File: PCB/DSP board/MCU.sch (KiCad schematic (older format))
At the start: 12 parts, among them J1 01x06 male SMD, U1 STM32H743II, Y1 ABS05-32.768, Y2 CX2016DB16000

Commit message: Schematics + Footprints Rev.1
Ready to route.
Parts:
- C1, C2, C3, C4, C5: footprint (none) -> Capacitors_SMD:C_0603
- J1: footprint (none) -> Pin_Headers:Pin_Header_Straight_1x06_Pitch2.54mm_SMD_Pin1Right
- R1: value 47k -> 12k; footprint (none) -> Resistors_SMD:R_0603
- R2: footprint (none) -> Resistors_SMD:R_0603
- S1: value Switch_SPST_4Pin -> FSM4JSMATR; footprint (none) -> Switch:FSM4JSMATR
- U1: footprint (none) -> Housings_QFP:LQFP-176_24x24mm_Pitch0.5mm
- Y1: footprint (none) -> Crystals:Crystal_SMD_MicroCrystal_CM9V-T1A-2pin_1.6x1.0mm
- Y2: footprint (none) -> Crystals:Crystal_SMD_2016-4pin_2.0x1.6mm
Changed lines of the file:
@@
 F 0 "U1" H 1600 3475 60  0000 C CNN
 F 1 "STM32H743II" H 1900 925 60  0000 C CNN
-F 2 "" H 1900 925 60  0001 C CNN
+F 2 "Housings_QFP:LQFP-176_24x24mm_Pitch0.5mm" H 1900 925 60  0001 C CNN
 F 3 "" H 1900 925 60  0001 C CNN
 	1    1900 2225
@@
 F 0 "U1" H 1600 6275 60  0000 C CNN
 F 1 "STM32H743II" H 1900 3725 60  0000 C CNN
-F 2 "" H 1900 3725 60  0001 C CNN
+F 2 "Housings_QFP:LQFP-176_24x24mm_Pitch0.5mm" H 1900 3725 60  0001 C CNN
 F 3 "" H 1900 3725 60  0001 C CNN
 	2    1900 5025
@@
 F 0 "U1" H 3650 3475 60  0000 C CNN
 F 1 "STM32H743II" H 3950 925 60  0000 C CNN
-F 2 "" H 3950 925 60  0001 C CNN
+F 2 "Housings_QFP:LQFP-176_24x24mm_Pitch0.5mm" H 3950 925 60  0001 C CNN
 F 3 "" H 3950 925 60  0001 C CNN
 	3    3950 2225
@@
 F 0 "U1" H 3700 6275 60  0000 C CNN
 F 1 "STM32H743II" H 4000 3725 60  0000 C CNN
-F 2 "" H 4000 3725 60  0001 C CNN
+F 2 "Housings_QFP:LQFP-176_24x24mm_Pitch0.5mm" H 4000 3725 60  0001 C CNN
 F 3 "" H 4000 3725 60  0001 C CNN
 	4    4000 5025
@@
 F 0 "U1" H 5700 3475 60  0000 C CNN
 F 1 "STM32H743II" H 6000 925 60  0000 C CNN
-F 2 "" H 6000 925 60  0001 C CNN
+F 2 "Housings_QFP:LQFP-176_24x24mm_Pitch0.5mm" H 6000 925 60  0001 C CNN
 F 3 "" H 6000 925 60  0001 C CNN
 	5    6000 2225
@@
 F 0 "U1" H 5750 6375 60  0000 C CNN
 F 1 "STM32H743II" H 6050 3825 60  0000 C CNN
-F 2 "" H 6050 3825 60  0001 C CNN
+F 2 "Housings_QFP:LQFP-176_24x24mm_Pitch0.5mm" H 6050 3825 60  0001 C CNN
 F 3 "" H 6050 3825 60  0001 C CNN
 	6    6050 5125
@@
 F 0 "U1" H 7700 3475 60  0000 C CNN
 F 1 "STM32H743II" H 8000 925 60  0000 C CNN
-F 2 "" H 8000 925 60  0001 C CNN
+F 2 "Housings_QFP:LQFP-176_24x24mm_Pitch0.5mm" H 8000 925 60  0001 C CNN
 F 3 "" H 8000 925 60  0001 C CNN
 	7    8000 2225
@@
 F 0 "U1" H 7750 6375 60  0000 C CNN
 F 1 "STM32H743II" H 8050 3825 60  0000 C CNN
-F 2 "" H 8050 3825 60  0001 C CNN
+F 2 "Housings_QFP:LQFP-176_24x24mm_Pitch0.5mm" H 8050 3825 60  0001 C CNN
 F 3 "" H 8050 3825 60  0001 C CNN
 	8    8050 5125
@@
 F 0 "U1" H 10400 3450 60  0000 C CNN
 F 1 "STM32H743II" H 10700 900 60  0000 C CNN
-F 2 "" H 10700 900 60  0001 C CNN
+F 2 "Housings_QFP:LQFP-176_24x24mm_Pitch0.5mm" H 10700 900 60  0001 C CNN
 F 3 "" H 10700 900 60  0001 C CNN
 	9    10700 2200
@@
 F 0 "C1" V 2725 3250 50  0000 L CNN
 F 1 "18pF" V 2625 2950 50  0000 L CNN
-F 2 "" H 2675 3200 50  0001 C CNN
+F 2 "Capacitors_SMD:C_0603" H 2675 3200 50  0001 C CNN
 F 3 "" H 2675 3200 50  0001 C CNN
 	1    2675 3200
@@
 F 0 "C2" V 2725 3450 50  0000 L CNN
 F 1 "18pF" V 2625 3150 50  0000 L CNN
-F 2 "" H 2675 3400 50  0001 C CNN
+F 2 "Capacitors_SMD:C_0603" H 2675 3400 50  0001 C CNN
 F 3 "" H 2675 3400 50  0001 C CNN
 	1    2675 3400
@@
 $EndComp
 $Comp
-L GND #PWR7
+L GND #PWR07
 U 1 1 5AABABFC
 P 2475 3500
-F 0 "#PWR7" H 2475 3250 50  0001 C CNN
+F 0 "#PWR07" H 2475 3250 50  0001 C CNN
 F 1 "GND" H 2475 3350 50  0000 C CNN
 F 2 "" H 2475 3500 50  0001 C CNN
@@
 F 0 "Y2" V 7000 3875 50  0000 L CNN
 F 1 "CX2016DB16000" V 6800 3825 50  0000 L CNN
-F 2 "" H 7150 4075 50  0001 C CNN
+F 2 "Crystals:Crystal_SMD_2016-4pin_2.0x1.6mm" H 7150 4075 50  0001 C CNN
 F 3 "" H 7150 4075 50  0001 C CNN
 	1    7150 4075
@@
 $EndComp
 $Comp
-L GND #PWR9
+L GND #PWR08
 U 1 1 5AABD6EF
 P 7350 4075
-F 0 "#PWR9" H 7350 3825 50  0001 C CNN
+F 0 "#PWR08" H 7350 3825 50  0001 C CNN
 F 1 "GND" H 7350 3925 50  0000 C CNN
 F 2 "" H 7350 4075 50  0001 C CNN
@@
 F 0 "Y1" V 3000 3400 50  0000 C CNN
 F 1 "ABS05-32.768" V 3300 3350 50  0000 C CNN
-F 2 "" H 3050 3300 50  0001 C CNN
+F 2 "Crystals:Crystal_SMD_MicroCrystal_CM9V-T1A-2pin_1.6x1.0mm" H 3050 3300 50  0001 C CNN
 F 3 "" H 3050 3300 50  0001 C CNN
 	1    3050 3300
@@
 F 0 "C3" V 6850 4025 50  0000 L CNN
 F 1 "18pF" V 6750 3725 50  0000 L CNN
-F 2 "" H 6800 3975 50  0001 C CNN
+F 2 "Capacitors_SMD:C_0603" H 6800 3975 50  0001 C CNN
 F 3 "" H 6800 3975 50  0001 C CNN
 	1    6800 3975
@@
 F 0 "C4" V 6850 4225 50  0000 L CNN
 F 1 "18pF" V 6750 3925 50  0000 L CNN
-F 2 "" H 6800 4175 50  0001 C CNN
+F 2 "Capacitors_SMD:C_0603" H 6800 4175 50  0001 C CNN
 F 3 "" H 6800 4175 50  0001 C CNN
 	1    6800 4175
@@
 $EndComp
 $Comp
-L GND #PWR8
+L GND #PWR09
 U 1 1 5AABF2BF
 P 6600 4275
-F 0 "#PWR8" H 6600 4025 50  0001 C CNN
+F 0 "#PWR09" H 6600 4025 50  0001 C CNN
 F 1 "GND" H 6600 4125 50  0000 C CNN
 F 2 "" H 6600 4275 50  0001 C CNN
@@
 F 0 "C5" H 8875 3275 50  0000 L CNN
 F 1 "100nF" H 8850 3125 50  0000 L CNN
-F 2 "" H 9100 3200 50  0001 C CNN
+F 2 "Capacitors_SMD:C_0603" H 9100 3200 50  0001 C CNN
 F 3 "" H 9100 3200 50  0001 C CNN
 	1    9100 3200
@@
 P 9300 3200
 F 0 "R1" H 9200 3275 50  0000 C CNN
-F 1 "47k" V 9300 3200 50  0000 C CNN
-F 2 "" V 9230 3200 50  0001 C CNN
+F 1 "12k" V 9300 3200 50  0000 C CNN
+F 2 "Resistors_SMD:R_0603" V 9230 3200 50  0001 C CNN
 F 3 "" H 9300 3200 50  0001 C CNN
 	1    9300 3200
@@
 Connection ~ 9100 2900
 $Comp
-L GND #PWR10
+L GND #PWR010
 U 1 1 5AAD2FCE
 P 9200 3475
-F 0 "#PWR10" H 9200 3225 50  0001 C CNN
+F 0 "#PWR010" H 9200 3225 50  0001 C CNN
 F 1 "GND" H 9200 3325 50  0000 C CNN
 F 2 "" H 9200 3475 50  0001 C CNN
@@
 F 0 "J1" H 10525 4375 50  0000 C CNN
 F 1 "01x06 male SMD" H 10475 3700 50  0000 C CNN
-F 2 "" H 10525 4075 50  0001 C CNN
+F 2 "Pin_Headers:Pin_Header_Straight_1x06_Pitch2.54mm_SMD_Pin1Right" H 10525 4075 50  0001 C CNN
 F 3 "" H 10525 4075 50  0001 C CNN
 	1    10525 4075
@@
 	10325 3875 10100 3875
 $Comp
-L GND #PWR11
+L GND #PWR011
 U 1 1 5AB64D9A
 P 10250 4075
-F 0 "#PWR11" H 10250 3825 50  0001 C CNN
+F 0 "#PWR011" H 10250 3825 50  0001 C CNN
 F 1 "GND" V 10250 3800 50  0000 C CNN
 F 2 "" H 10250 4075 50  0001 C CNN
@@
 P 10200 4950
 F 0 "S1" V 10475 4950 60  0000 C CNN
-F 1 "Switch_SPST_4Pin" V 9950 4925 60  0000 C CNN
-F 2 "" H 10000 5050 60  0001 C CNN
+F 1 "FSM4JSMATR" V 9950 4925 60  0000 C CNN
+F 2 "Switch:FSM4JSMATR" H 10000 5050 60  0001 C CNN
 F 3 "" H 10000 5050 60  0001 C CNN
 	1    10200 4950
@@
 F 0 "R2" V 10780 5100 50  0000 C CNN
 F 1 "820R" V 10700 5100 50  0000 C CNN
-F 2 "" V 10630 5100 50  0001 C CNN
+F 2 "Resistors_SMD:R_0603" V 10630 5100 50  0001 C CNN
 F 3 "" H 10700 5100 50  0001 C CNN
 	1    10700 5100
@@
 $EndComp
 $Comp
-L GND #PWR12
+L GND #PWR012
 U 1 1 5AB64DB1
 P 10925 5150
-F 0 "#PWR12" H 10925 4900 50  0001 C CNN
+F 0 "#PWR012" H 10925 4900 50  0001 C CNN
 F 1 "GND" H 10925 5000 50  0000 C CNN
 F 2 "" H 10925 5150 50  0001 C CNN

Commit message: Schematics & PCB
Schematics update - ERC error fixing
PCB - setup & PCB outline
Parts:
- renumbered C1 to C201, C2 to C202, C3 to C203, C4 to C204, C5 to C205, J1 to J201, R1 to R201, R2 to R202, S1 to S201, U1 to U201, Y1 to Y201, Y2 to Y202
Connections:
- no-connect marks 0 -> 14
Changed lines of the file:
@@
 $EndSheet
 $Comp
-L STM32H743II U1
+L STM32H743II U201
 U 1 1 5AAA3D93
 P 1900 2225
-F 0 "U1" H 1600 3475 60  0000 C CNN
+F 0 "U201" H 1600 3475 60  0000 C CNN
 F 1 "STM32H743II" H 1900 925 60  0000 C CNN
 F 2 "Housings_QFP:LQFP-176_24x24mm_Pitch0.5mm" H 1900 925 60  0001 C CNN
@@
 $EndComp
 $Comp
-L STM32H743II U1
+L STM32H743II U201
 U 2 1 5AAA3F85
 P 1900 5025
-F 0 "U1" H 1600 6275 60  0000 C CNN
+F 0 "U201" H 1600 6275 60  0000 C CNN
 F 1 "STM32H743II" H 1900 3725 60  0000 C CNN
 F 2 "Housings_QFP:LQFP-176_24x24mm_Pitch0.5mm" H 1900 3725 60  0001 C CNN
@@
 $EndComp
 $Comp
-L STM32H743II U1
+L STM32H743II U201
 U 3 1 5AAA4068
 P 3950 2225
-F 0 "U1" H 3650 3475 60  0000 C CNN
+F 0 "U201" H 3650 3475 60  0000 C CNN
 F 1 "STM32H743II" H 3950 925 60  0000 C CNN
 F 2 "Housings_QFP:LQFP-176_24x24mm_Pitch0.5mm" H 3950 925 60  0001 C CNN
@@
 $EndComp
 $Comp
-L STM32H743II U1
+L STM32H743II U201
 U 4 1 5AAA418D
 P 4000 5025
-F 0 "U1" H 3700 6275 60  0000 C CNN
+F 0 "U201" H 3700 6275 60  0000 C CNN
 F 1 "STM32H743II" H 4000 3725 60  0000 C CNN
 F 2 "Housings_QFP:LQFP-176_24x24mm_Pitch0.5mm" H 4000 3725 60  0001 C CNN
@@
 $EndComp
 $Comp
-L STM32H743II U1
+L STM32H743II U201
 U 5 1 5AAA4260
 P 6000 2225
-F 0 "U1" H 5700 3475 60  0000 C CNN
+F 0 "U201" H 5700 3475 60  0000 C CNN
 F 1 "STM32H743II" H 6000 925 60  0000 C CNN
 F 2 "Housings_QFP:LQFP-176_24x24mm_Pitch0.5mm" H 6000 925 60  0001 C CNN
@@
 $EndComp
 $Comp
-L STM32H743II U1
+L STM32H743II U201
 U 6 1 5AAA44FA
 P 6050 5125
-F 0 "U1" H 5750 6375 60  0000 C CNN
+F 0 "U201" H 5750 6375 60  0000 C CNN
 F 1 "STM32H743II" H 6050 3825 60  0000 C CNN
 F 2 "Housings_QFP:LQFP-176_24x24mm_Pitch0.5mm" H 6050 3825 60  0001 C CNN
@@
 $EndComp
 $Comp
-L STM32H743II U1
+L STM32H743II U201
 U 7 1 5AAA45B7
 P 8000 2225
-F 0 "U1" H 7700 3475 60  0000 C CNN
+F 0 "U201" H 7700 3475 60  0000 C CNN
 F 1 "STM32H743II" H 8000 925 60  0000 C CNN
 F 2 "Housings_QFP:LQFP-176_24x24mm_Pitch0.5mm" H 8000 925 60  0001 C CNN
@@
 $EndComp
 $Comp
-L STM32H743II U1
+L STM32H743II U201
 U 8 1 5AAA4638
 P 8050 5125
-F 0 "U1" H 7750 6375 60  0000 C CNN
+F 0 "U201" H 7750 6375 60  0000 C CNN
 F 1 "STM32H743II" H 8050 3825 60  0000 C CNN
 F 2 "Housings_QFP:LQFP-176_24x24mm_Pitch0.5mm" H 8050 3825 60  0001 C CNN
@@
 $EndComp
 $Comp
-L STM32H743II U1
+L STM32H743II U201
 U 9 1 5AAA46D7
 P 10700 2200
-F 0 "U1" H 10400 3450 60  0000 C CNN
+F 0 "U201" H 10400 3450 60  0000 C CNN
 F 1 "STM32H743II" H 10700 900 60  0000 C CNN
 F 2 "Housings_QFP:LQFP-176_24x24mm_Pitch0.5mm" H 10700 900 60  0001 C CNN
@@
 NRST
 $Comp
-L C_Small C1
+L C_Small C201
 U 1 1 5AABA6FC
 P 2675 3200
-F 0 "C1" V 2725 3250 50  0000 L CNN
+F 0 "C201" V 2725 3250 50  0000 L CNN
 F 1 "18pF" V 2625 2950 50  0000 L CNN
 F 2 "Capacitors_SMD:C_0603" H 2675 3200 50  0001 C CNN
@@
 $EndComp
 $Comp
-L C_Small C2
+L C_Small C202
 U 1 1 5AABA76F
 P 2675 3400
-F 0 "C2" V 2725 3450 50  0000 L CNN
+F 0 "C202" V 2725 3450 50  0000 L CNN
 F 1 "18pF" V 2625 3150 50  0000 L CNN
 F 2 "Capacitors_SMD:C_0603" H 2675 3400 50  0001 C CNN
@@
 $EndComp
 $Comp
-L GND #PWR07
+L GND #PWR08
 U 1 1 5AABABFC
 P 2475 3500
-F 0 "#PWR07" H 2475 3250 50  0001 C CNN
+F 0 "#PWR08" H 2475 3250 50  0001 C CNN
 F 1 "GND" H 2475 3350 50  0000 C CNN
 F 2 "" H 2475 3500 50  0001 C CNN
@@
 $EndComp
 $Comp
-L Crystal_GND24_Small Y2
+L Crystal_GND24_Small Y202
 U 1 1 5AABB474
 P 7150 4075
-F 0 "Y2" V 7000 3875 50  0000 L CNN
+F 0 "Y202" V 7000 3875 50  0000 L CNN
 F 1 "CX2016DB16000" V 6800 3825 50  0000 L CNN
 F 2 "Crystals:Crystal_SMD_2016-4pin_2.0x1.6mm" H 7150 4075 50  0001 C CNN
@@
 $EndComp
 $Comp
-L GND #PWR08
+L GND #PWR09
 U 1 1 5AABD6EF
 P 7350 4075
-F 0 "#PWR08" H 7350 3825 50  0001 C CNN
+F 0 "#PWR09" H 7350 3825 50  0001 C CNN
 F 1 "GND" H 7350 3925 50  0000 C CNN
 F 2 "" H 7350 4075 50  0001 C CNN
@@
 $EndComp
 $Comp
-L Crystal_Small Y1
+L Crystal_Small Y201
 U 1 1 5AABC242
 P 3050 3300
-F 0 "Y1" V 3000 3400 50  0000 C CNN
+F 0 "Y201" V 3000 3400 50  0000 C CNN
 F 1 "ABS05-32.768" V 3300 3350 50  0000 C CNN
 F 2 "Crystals:Crystal_SMD_MicroCrystal_CM9V-T1A-2pin_1.6x1.0mm" H 3050 3300 50  0001 C CNN
@@
 $EndComp
 $Comp
-L C_Small C3
+L C_Small C203
 U 1 1 5AABF2B3
 P 6800 3975
-F 0 "C3" V 6850 4025 50  0000 L CNN
+F 0 "C203" V 6850 4025 50  0000 L CNN
 F 1 "18pF" V 6750 3725 50  0000 L CNN
 F 2 "Capacitors_SMD:C_0603" H 6800 3975 50  0001 C CNN
@@
 $EndComp
 $Comp
-L C_Small C4
+L C_Small C204
 U 1 1 5AABF2B9
 P 6800 4175
-F 0 "C4" V 6850 4225 50  0000 L CNN
+F 0 "C204" V 6850 4225 50  0000 L CNN
 F 1 "18pF" V 6750 3925 50  0000 L CNN
 F 2 "Capacitors_SMD:C_0603" H 6800 4175 50  0001 C CNN
@@
 $EndComp
 $Comp
-L GND #PWR09
+L GND #PWR010
 U 1 1 5AABF2BF
 P 6600 4275
-F 0 "#PWR09" H 6600 4025 50  0001 C CNN
+F 0 "#PWR010" H 6600 4025 50  0001 C CNN
 F 1 "GND" H 6600 4125 50  0000 C CNN
 F 2 "" H 6600 4275 50  0001 C CNN
@@
 	9950 2750 10100 2750
 $Comp
-L C_Small C5
+L C_Small C205
 U 1 1 5AAD04A7
 P 9100 3200
-F 0 "C5" H 8875 3275 50  0000 L CNN
+F 0 "C205" H 8875 3275 50  0000 L CNN
 F 1 "100nF" H 8850 3125 50  0000 L CNN
 F 2 "Capacitors_SMD:C_0603" H 9100 3200 50  0001 C CNN
@@
 $EndComp
 $Comp
-L R R1
+L R R201
 U 1 1 5AAD057A
 P 9300 3200
-F 0 "R1" H 9200 3275 50  0000 C CNN
+F 0 "R201" H 9200 3275 50  0000 C CNN
 F 1 "12k" V 9300 3200 50  0000 C CNN
 F 2 "Resistors_SMD:R_0603" V 9230 3200 50  0001 C CNN
@@
 Connection ~ 9100 2900
 $Comp
-L GND #PWR010
+L GND #PWR011
 U 1 1 5AAD2FCE
 P 9200 3475
-F 0 "#PWR010" H 9200 3225 50  0001 C CNN
+F 0 "#PWR011" H 9200 3225 50  0001 C CNN
 F 1 "GND" H 9200 3325 50  0000 C CNN
 F 2 "" H 9200 3475 50  0001 C CNN
@@
 	9950 3200 10100 3200
 $Comp
-L Conn_01x06_Male J1
+L Conn_01x06_Male J201
 U 1 1 5AB64D89
 P 10525 4075
-F 0 "J1" H 10525 4375 50  0000 C CNN
+F 0 "J201" H 10525 4375 50  0000 C CNN
 F 1 "01x06 male SMD" H 10475 3700 50  0000 C CNN
 F 2 "Pin_Headers:Pin_Header_Straight_1x06_Pitch2.54mm_SMD_Pin1Right" H 10525 4075 50  0001 C CNN
@@
 	10325 3875 10100 3875
 $Comp
-L GND #PWR011
+L GND #PWR012
 U 1 1 5AB64D9A
 P 10250 4075
-F 0 "#PWR011" H 10250 3825 50  0001 C CNN
+F 0 "#PWR012" H 10250 3825 50  0001 C CNN
 F 1 "GND" V 10250 3800 50  0000 C CNN
 F 2 "" H 10250 4075 50  0001 C CNN
@@
 	10250 4075 10325 4075
 $Comp
-L Switch_SPST_4Pin S1
+L Switch_SPST_4Pin S201
 U 1 1 5AB64DA1
 P 10200 4950
-F 0 "S1" V 10475 4950 60  0000 C CNN
+F 0 "S201" V 10475 4950 60  0000 C CNN
 F 1 "FSM4JSMATR" V 9950 4925 60  0000 C CNN
 F 2 "Switch:FSM4JSMATR" H 10000 5050 60  0001 C CNN
@@
 	9800 4800 9950 4800
 $Comp
-L R R2
+L R R202
 U 1 1 5AB64DAA
 P 10700 5100
-F 0 "R2" V 10780 5100 50  0000 C CNN
+F 0 "R202" V 10780 5100 50  0000 C CNN
 F 1 "820R" V 10700 5100 50  0000 C CNN
 F 2 "Resistors_SMD:R_0603" V 10630 5100 50  0001 C CNN
@@
 $EndComp
 $Comp
-L GND #PWR012
+L GND #PWR013
 U 1 1 5AB64DB1
 P 10925 5150
-F 0 "#PWR012" H 10925 4900 50  0001 C CNN
+F 0 "#PWR013" H 10925 4900 50  0001 C CNN
 F 1 "GND" H 10925 5000 50  0000 C CNN
 F 2 "" H 10925 5150 50  0001 C CNN
@@
 Text Notes 10300 7500 0    60   ~ 0
 By Jesse Spiessens
+NoConn ~ 1300 4525
+NoConn ~ 3350 1425
+NoConn ~ 3350 1575
+NoConn ~ 3400 4375
+NoConn ~ 5400 1275
+NoConn ~ 7400 1575
+NoConn ~ 7450 4475
+NoConn ~ 7450 4925
+NoConn ~ 7450 5075
+NoConn ~ 10100 1550
+NoConn ~ 10100 3350
+NoConn ~ 9950 5100
+NoConn ~ 10450 4800
+NoConn ~ 1300 3375
 $EndSCHEMATC

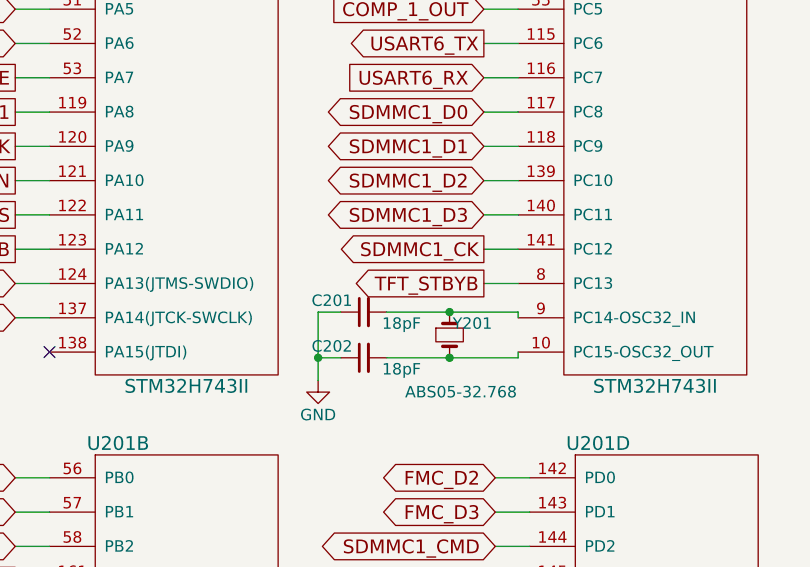
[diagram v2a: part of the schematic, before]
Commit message: RAM Routing - Data
All RAM routing & matching done, supply still needs to be done
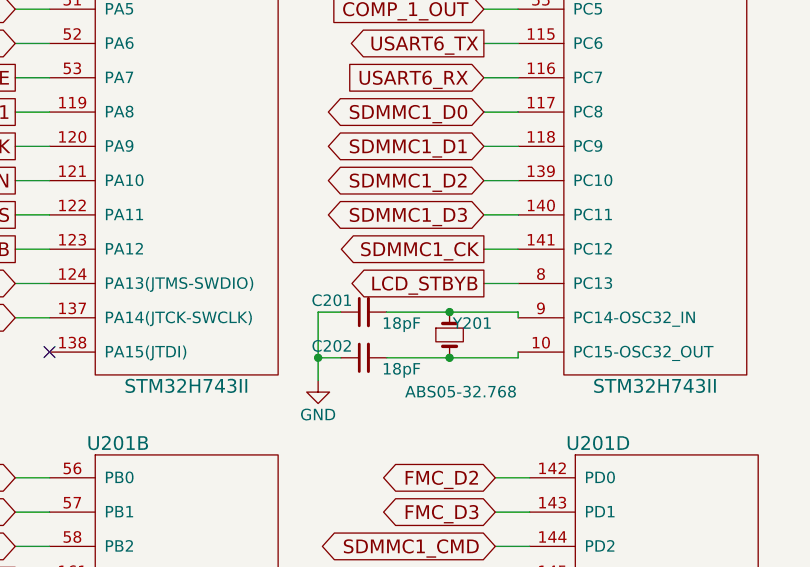
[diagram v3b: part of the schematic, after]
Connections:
- net TFT_STBYB renamed LCD_STBYB
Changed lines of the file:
@@
 	3400 5425 3250 5425
 Text GLabel 3200 3075 0    60   Output ~ 0
-TFT_STBYB
+LCD_STBYB
 Wire Wire Line
 	3200 3075 3350 3075

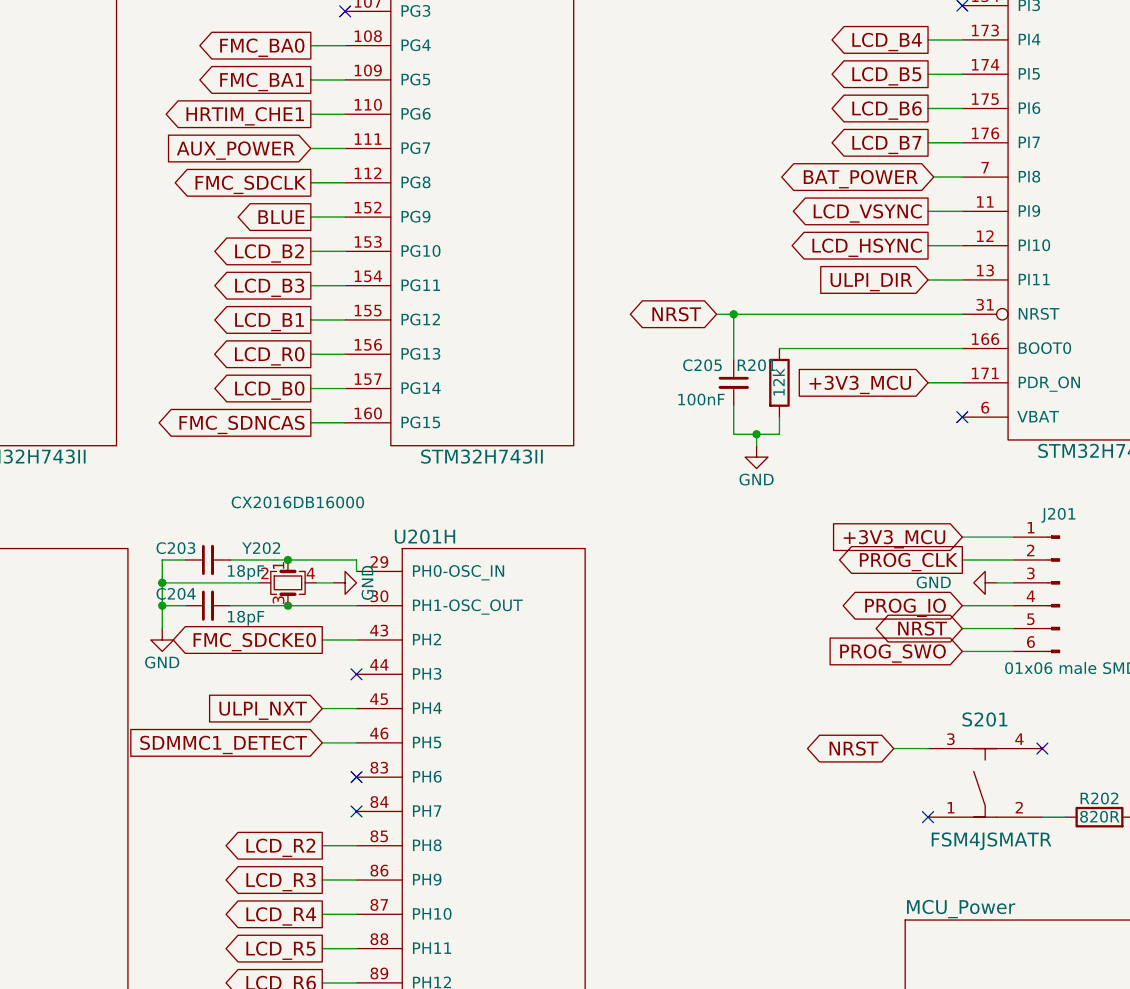
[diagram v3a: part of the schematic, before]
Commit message: RAM + Display
Ram & display routed + matched-ish
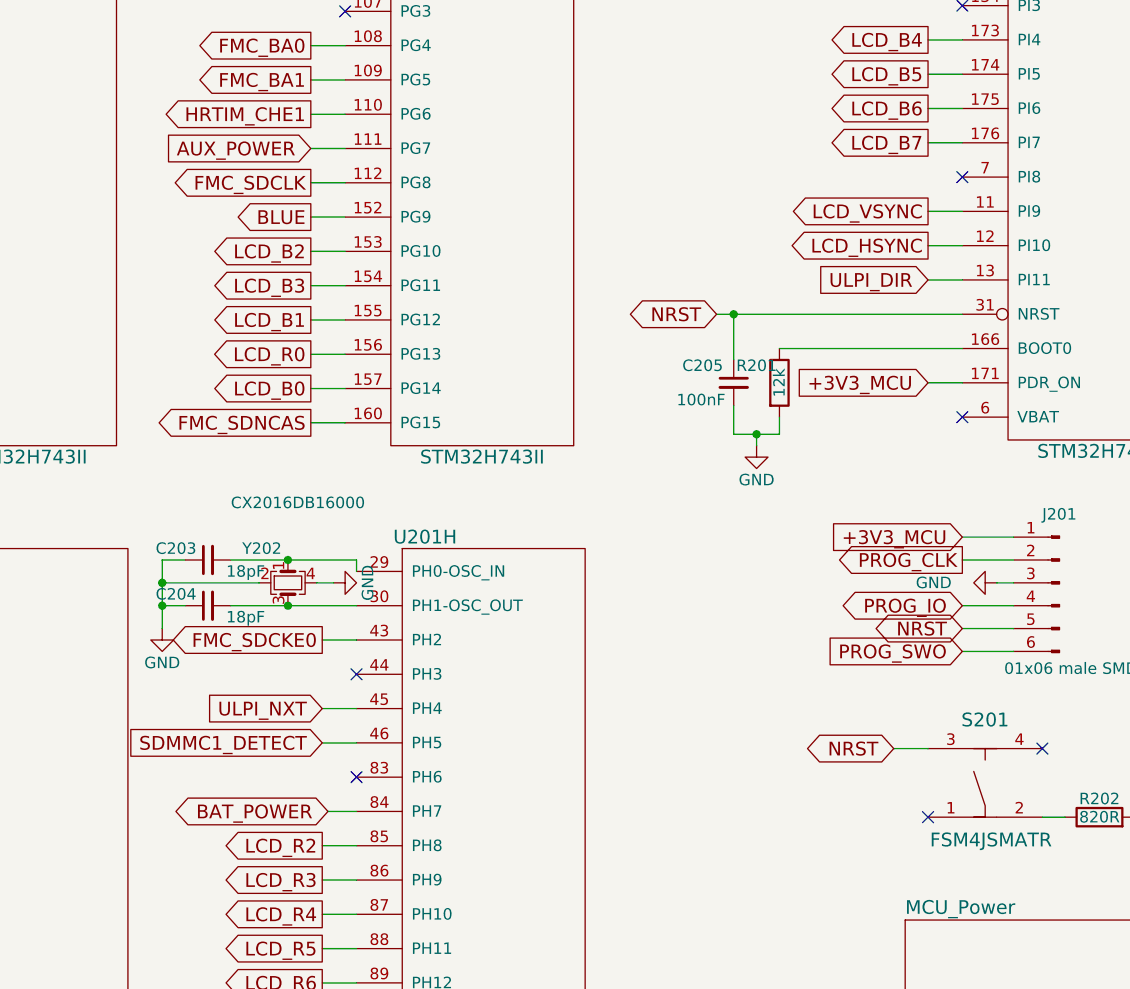
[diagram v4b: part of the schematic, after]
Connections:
- net BAT_POWER: now also U201.84 (PH7); no longer U201.7 (PI8)
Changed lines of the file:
@@
 Wire Wire Line
 	10100 3050 9300 3050
-Text GLabel 9975 2300 0    60   BiDi ~ 0
+Text GLabel 7325 5075 0    60   BiDi ~ 0
 BAT_POWER
 Wire Wire Line
-	9975 2300 10100 2300
+	7325 5075 7450 5075
 Text GLabel 9950 3200 0    60   Input ~ 0
 +3V3_MCU
@@
 NoConn ~ 7450 4475
 NoConn ~ 7450 4925
-NoConn ~ 7450 5075
 NoConn ~ 10100 1550
 NoConn ~ 10100 3350
@@
 NoConn ~ 10450 4800
 NoConn ~ 1300 3375
+NoConn ~ 10100 2300
 $EndSCHEMATC
